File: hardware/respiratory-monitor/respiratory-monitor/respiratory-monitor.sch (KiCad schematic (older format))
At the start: 6 parts

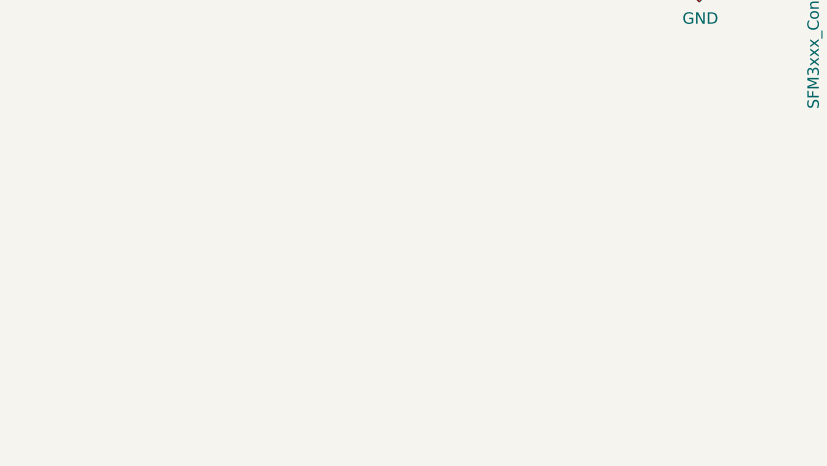
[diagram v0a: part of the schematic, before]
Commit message: Add the pressure sensor
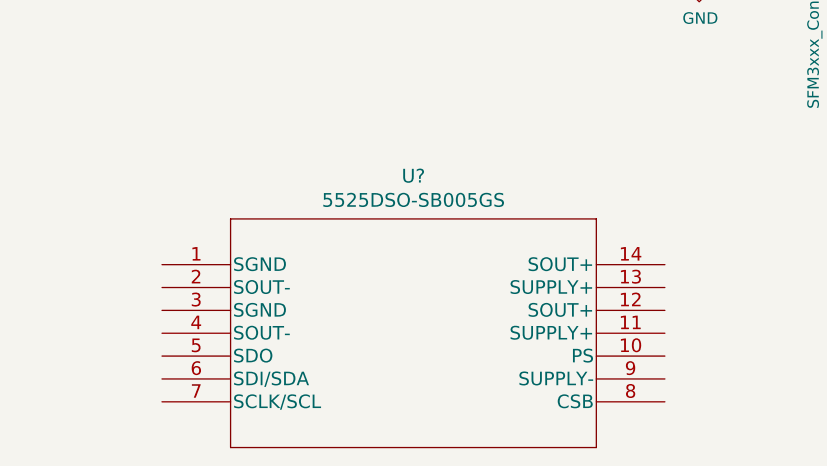
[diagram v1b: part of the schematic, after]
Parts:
- added U?: 5525DSO-SB005GS, SO14_MS5525DSO, symbol proj-components:5525DSO-SB005GS
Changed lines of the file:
@@
 	2950 1650 3250 1650
 Connection ~ 2950 1650
+$Comp
+L proj-components:5525DSO-SB005GS U?
+U 1 1 5E97BD83
+P 3400 3500
+F 0 "U?" H 4500 3887 60  0000 C CNN
+F 1 "5525DSO-SB005GS" H 4500 3781 60  0000 C CNN
+F 2 "SO14_MS5525DSO" H 4500 3740 60  0001 C CNN
+F 3 "https://www.te.com/commerce/DocumentDelivery/DDEController?Action=srchrtrv&DocNm=MS5525DSO&DocType=DS&DocLang=English" H 4500 3781 60  0001 C CNN
+F 4 "https://www.digikey.com/product-detail/en/te-connectivity-measurement-specialties/5525DSO-SB005GS/223-1706-5-ND/5824907" H 3400 3500 50  0001 C CNN "DigiKey"
+F 5 "223-1706-5-ND" H 3400 3500 50  0001 C CNN "DigiKeyPartNumber"
+F 6 "TE Connectivity Measurement Specialties" H 3400 3500 50  0001 C CNN "Manufacturer"
+	1    3400 3500
+	1    0    0    -1
+$EndComp
 $EndSCHEMATC
